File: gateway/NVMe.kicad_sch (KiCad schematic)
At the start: 0 parts

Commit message: Working on PCB
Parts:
- added C1401, C1402, C1411: 10u, Capacitor_SMD:C_0805_2012Metric, symbol Device:C
- added C1403, C1405, C1408, C1409: 100n, Capacitor_SMD:C_0402_1005Metric, symbol Device:C
- added C1404: 68n, Capacitor_SMD:C_0402_1005Metric, symbol Device:C
- added C1406: 150p, Capacitor_SMD:C_0402_1005Metric, symbol Device:C
- added C1407: 470u, Capacitor_SMD:CP_Elec_6.3x7.7, symbol Device:C_Polarized
- added C1410: 33p, Capacitor_SMD:C_0402_1005Metric, symbol Device:C
- added D1403: STPS3L60U, Diode_SMD:D_SMB, symbol ST:STPS3L60U
- added H1401: MountingHole, Wuerth:9774025151R, symbol Mechanical_Kampi:MountingHole
- added IC1402: ST1S14PHR, Package_SO:HSOP-8-1EP_3.9x4.9mm_P1.27mm_EP2.41x3.1mm, symbol ST:ST1S14PHR
- added L1401: 10u, Inductor_SMD:L_Wuerth_HCI-7050, symbol Device:L
- added LED1401: Power Good, LED_SMD:LED_0805_2012Metric, symbol Device:LED
- added MP1401: (no value), Bivar:SLP3-300-100-F, symbol Mechanical_Kampi:Light_Pipe
- added R1401, R1402: 100k, Resistor_SMD:R_0402_1005Metric, symbol Device:R
- added R1403: 150R, Resistor_SMD:R_0402_1005Metric, symbol Device:R
- added R1404: 82k5, Resistor_SMD:R_0402_1005Metric, symbol Device:R
- added R1405: 48k7, Resistor_SMD:R_0402_1005Metric, symbol Device:R
- added R1406: 4k7, Resistor_SMD:R_0805_2012Metric, symbol Device:R
- added TP1401, TP1402, TP1403: (no value), Testpoints_Kampi:TestPoint_Pad_1.0x1.0mm, symbol Connector:TestPoint
- added X1401: SSD, Amphenol:MDT420M03001, symbol Connector:Bus_M.2_Socket_M
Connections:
- new net: C1406.2, IC1402.4 (FB), R1404.2, R1405.1, TP1402.1
- new net: IC1402.3 (~{EN1}), R1402.1
- new net: LED1401.2 (A), R1403.2
- new net: C1405.1, D1403.1 (K), IC1402.8 (SW), L1401.1
- new net: C1405.2, IC1402.1 (BOOT)
- new net: IC1402.2 (PG), LED1401.1 (K)
- new net +1V8: R1406.1
- new net GND: C1401.2, C1402.2, C1403.2, C1404.2, C1407.2, C1408.2, C1409.2, C1410.2, C1411.2, D1403.2 (A), IC1402.6 (GND), IC1402.9 (EP), R1401.2, R1402.2, R1405.2, X1401.1 (GND), X1401.15 (GND), X1401.21 (GND), X1401.27 (GND), X1401.3 (GND), X1401.33 (GND), X1401.39 (GND), X1401.45 (GND), X1401.51 (GND), X1401.57 (GND), X1401.71 (GND), X1401.73 (GND), X1401.75 (GND), X1401.9 (GND)
- new net PCIe.CLK_N: X1401.53 (REFCLKn)
- new net PCIe.CLK_P: X1401.55 (REFCLKp)
- new net PCIe.RX_N: X1401.41 (PERn0/SATA-B+)
- new net PCIe.RX_P: X1401.43 (PERp0/SATA-B-)
- new net PCIe.TX_N: X1401.47 (PETn0/SATA-A-)
- new net PCIe.TX_P: X1401.49 (PETp0/SATA-A+)
- new net PCIe.~{CLK-REQ}: X1401.50 (~{PERST})
- new net PCIe.~{RST}: X1401.52 (~{CLKREQ})
- new net SSD-Power: IC1402.5 (EN2), R1401.1
- new net V_{In}: C1401.1, C1402.1, C1403.1, C1404.1, IC1402.7 (VIN), TP1401.1
- new net V_{SSD}: C1406.1, C1407.1, C1408.1, C1409.1, C1410.1, C1411.1, L1401.2, R1403.1, R1404.1, TP1403.1, X1401.12 (3.3V), X1401.14 (3.3V), X1401.16 (3.3V), X1401.18 (3.3V), X1401.2 (3.3V), X1401.4 (3.3V), X1401.70 (3.3V), X1401.72 (3.3V), X1401.74 (3.3V)
- new net ~{CTRL_WAKE1_MICO}: R1406.2, X1401.54 (~{PEWAKE})
- no-connect marks 0 -> 16

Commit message: Working on version 1.0.0
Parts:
- H1401: footprint Wuerth:9774025151R -> Wuerth:9774015151R; manf# 9774025151R -> 9774015151R; mouser# 710-9774025151R -> 710-9774015151R
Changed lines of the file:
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@@
 			)
 		)
-		(property "Datasheet" "https://cdn.amphenol-cs.com/media/wysiwyg/files/drawing/mdtxxxxxx001.pdf"
+		(property "Datasheet" "https://web.archive.org/web/20200613074028/http://read.pudn.com/downloads794/doc/project/3133918/PCIe_M.2_Electromechanical_Spec_Rev1.0_Final_11012013_RS_Clean.pdf#page=155"
 			(at 215.9 144.78 0)
 			(hide yes)
@@
 			)
 		)
-		(property "Footprint" "Wuerth:9774025151R"
+		(property "Footprint" "Wuerth:9774015151R"
 			(at 201.93 278.13 0)
 			(hide yes)
@@
 			)
 		)
-		(property "Datasheet" "https://www.we-online.com/components/products/datasheet/9774025151R.pdf"
+		(property "Datasheet" "https://www.we-online.com/components/products/datasheet/9774015151R.pdf"
 			(at 201.93 278.13 0)
 			(hide yes)
@@
 			)
 		)
-		(property "manf#" "9774025151R"
+		(property "manf#" "9774015151R"
 			(at 201.93 278.13 0)
 			(hide yes)
@@
 			)
 		)
-		(property "mouser#" "710-9774025151R"
+		(property "mouser#" "710-9774015151R"
 			(at 201.93 278.13 0)
 			(hide yes)

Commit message: Working on version 1.0.0
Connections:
- net SSD-Power renamed SSD-Power-Enable
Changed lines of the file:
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@@
 		)
 	)
-	(hierarchical_label "SSD-Power"
+	(hierarchical_label "SSD-Power-Enable"
 		(shape input)
 		(at 64.77 124.46 180)

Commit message: Adding level shifter, update documentation
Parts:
- TP1401, TP1402, TP1403: value (none) -> ~
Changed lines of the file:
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@@
 			)
 		)
-		(property "Value" ""
+		(property "Value" "~"
 			(at 161.29 94.615 0)
 			(show_name no)
@@
 			)
 		)
-		(property "Value" ""
+		(property "Value" "~"
 			(at 62.23 66.675 0)
 			(show_name no)
@@
 			)
 		)
-		(property "Value" ""
+		(property "Value" "~"
 			(at 181.61 66.675 0)
 			(show_name no)

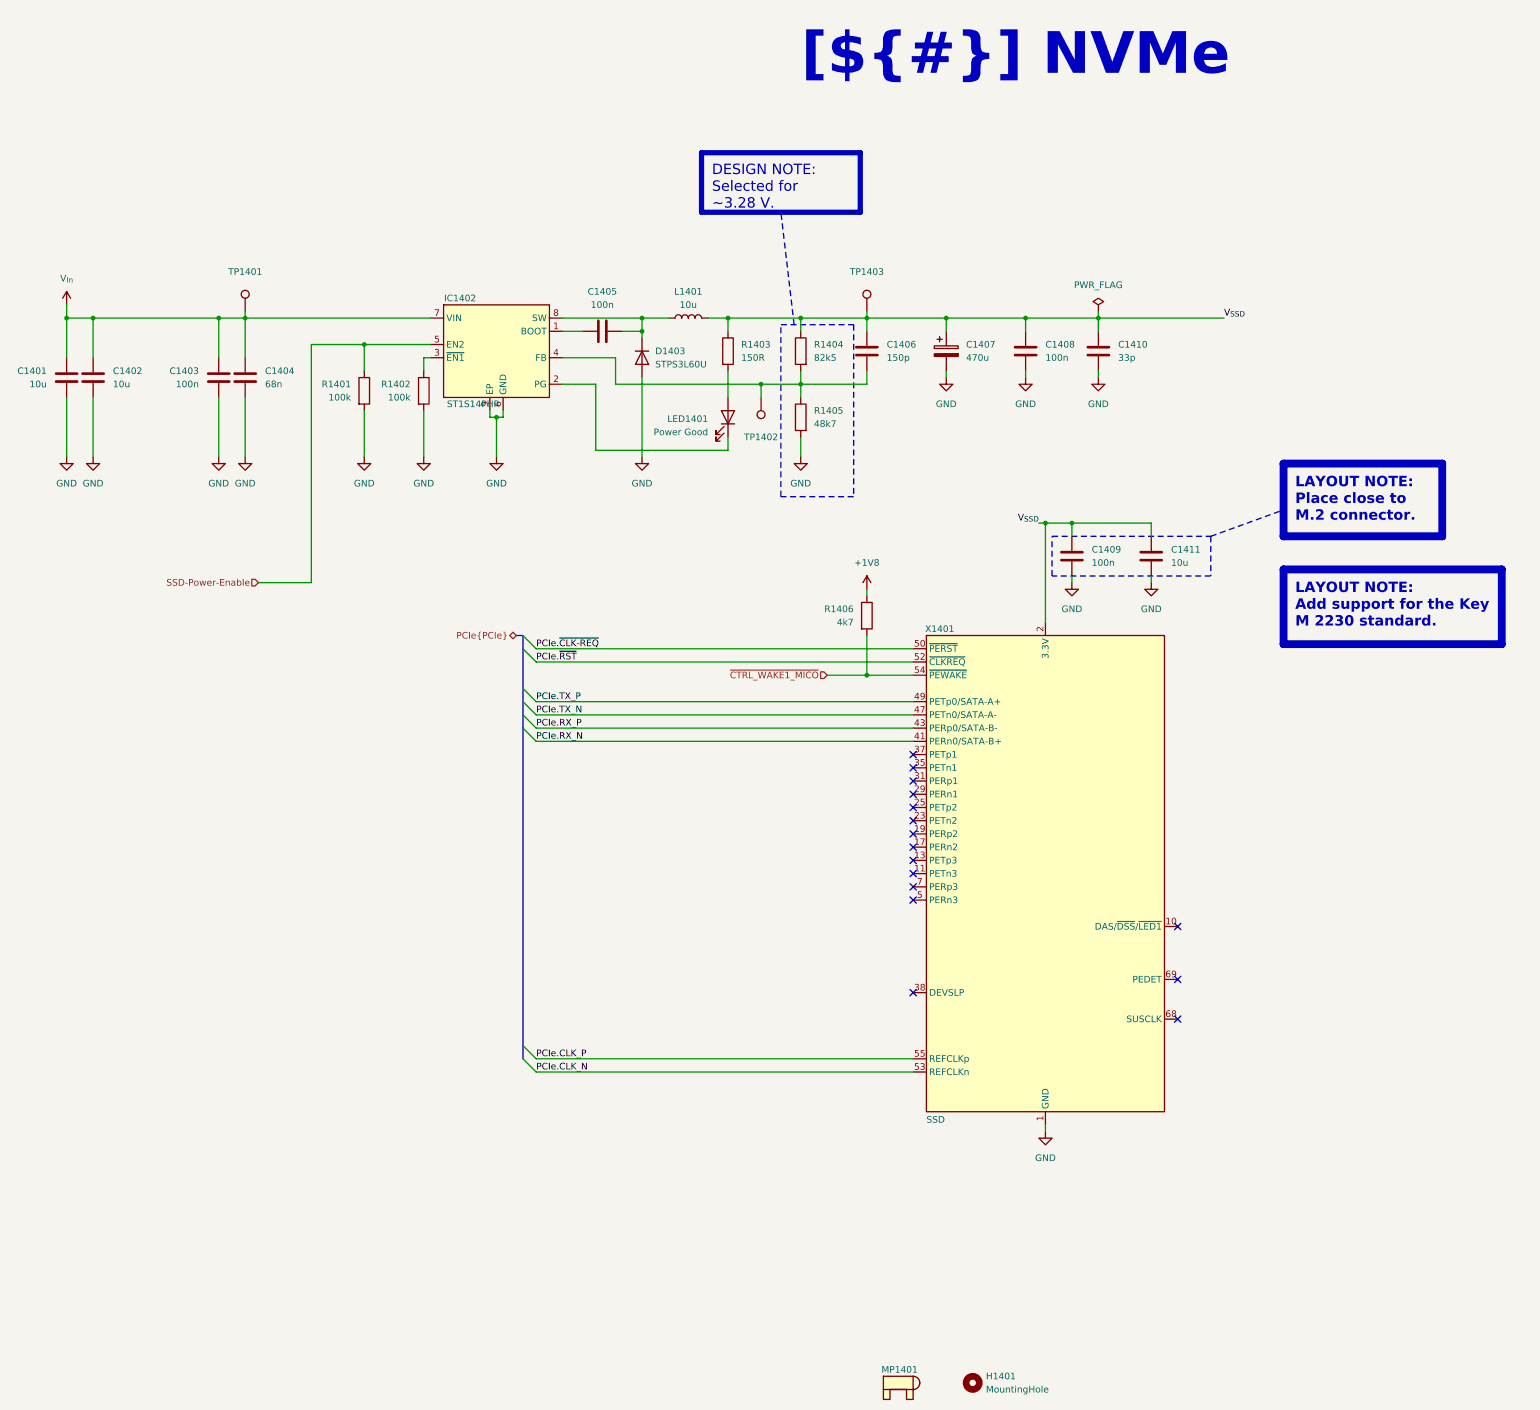
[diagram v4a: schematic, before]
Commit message: Replace level shifter, replace CC2530 with CC2652, fix wrong part numbers
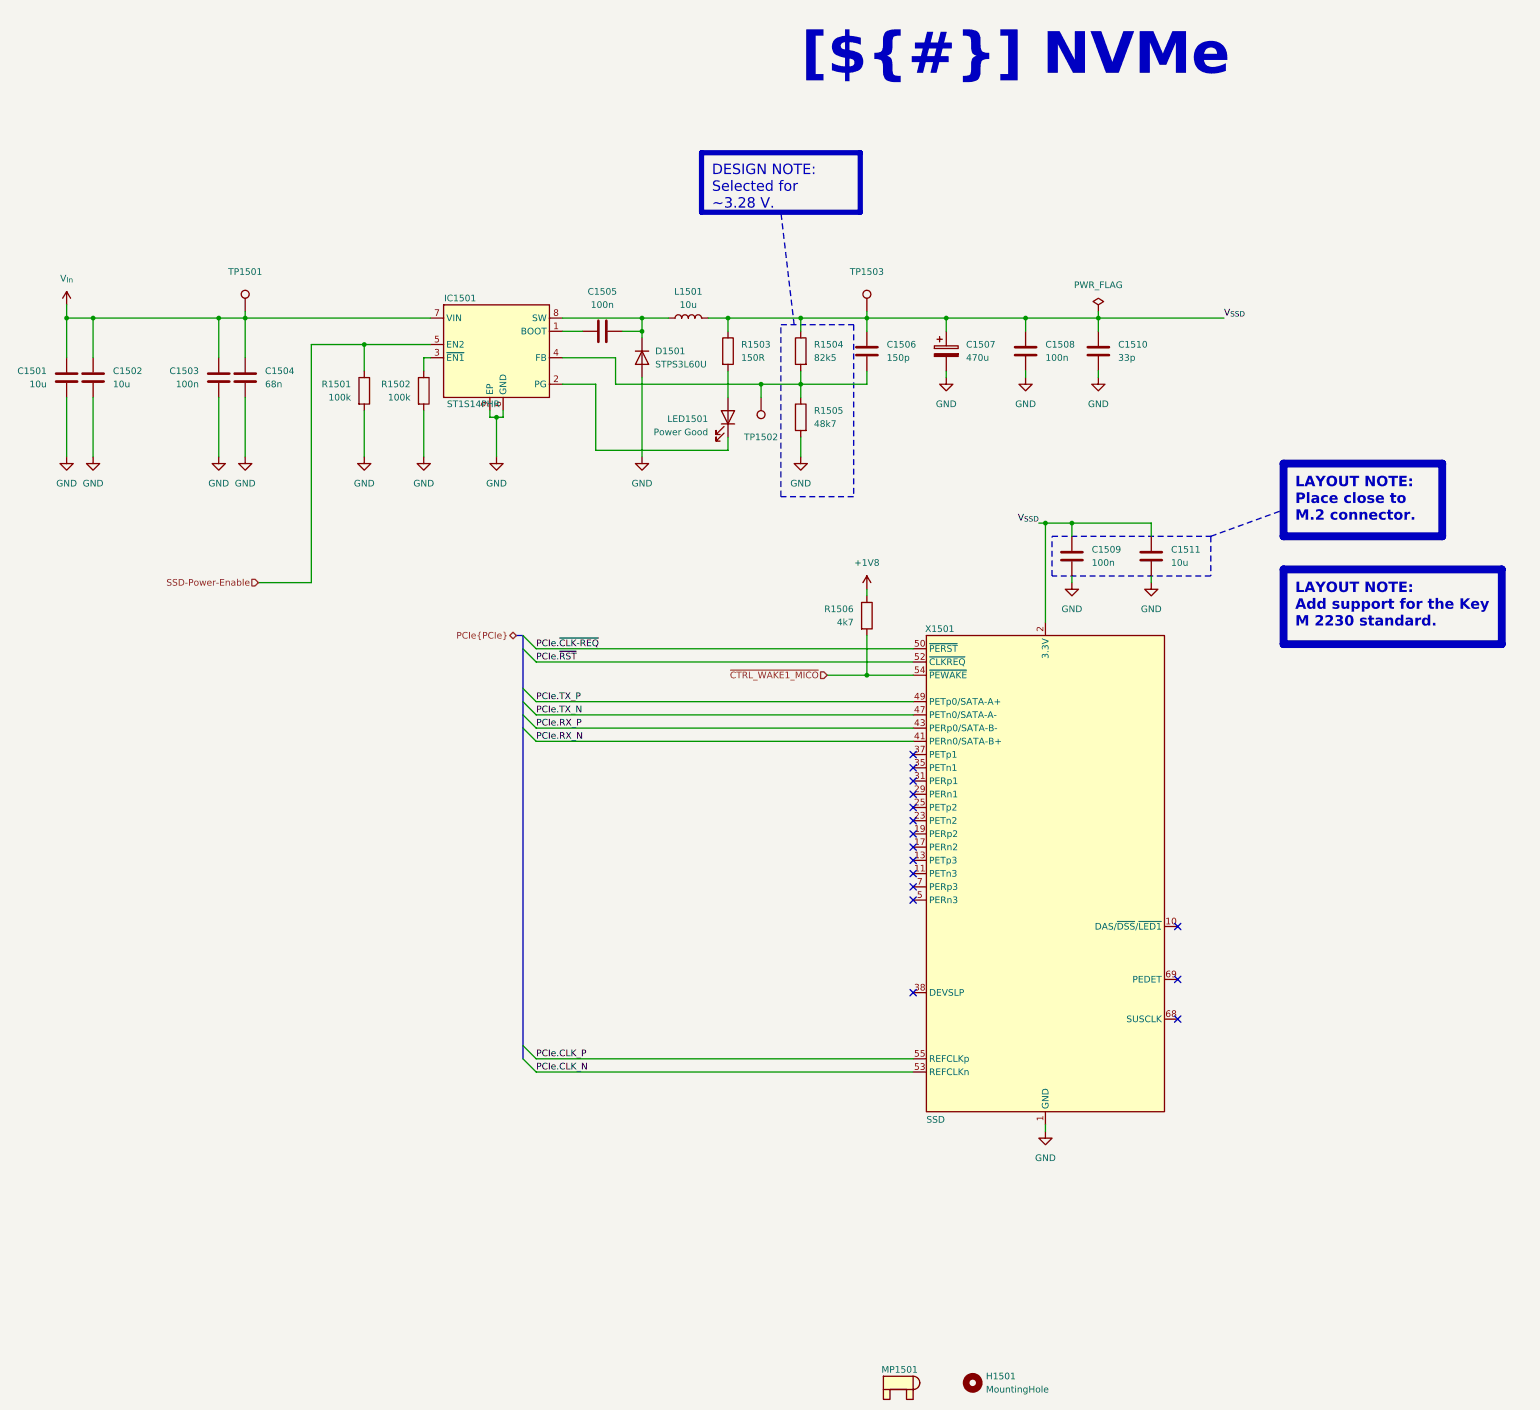
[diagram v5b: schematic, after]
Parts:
- C1503: renamed from C1403; footprint Capacitor_SMD:C_0402_1005Metric -> Capacitor_SMD:C_0805_2012Metric; manf# 04025C104JAT2A -> 08053C104M4T4A
- C1504: renamed from C1404; footprint Capacitor_SMD:C_0402_1005Metric -> Capacitor_SMD:C_0805_2012Metric; manf# 04025C683KAT2A -> 0805YC683KAT2A
- C1505: renamed from C1405; footprint Capacitor_SMD:C_0402_1005Metric -> Capacitor_SMD:C_0805_2012Metric; manf# 04025C104JAT2A -> 08053C104M4T4A
- C1506: renamed from C1406; footprint Capacitor_SMD:C_0402_1005Metric -> Capacitor_SMD:C_0805_2012Metric; manf# 04025C151MAT2A -> 08051U151JAT2A
- C1508: renamed from C1408; footprint Capacitor_SMD:C_0402_1005Metric -> Capacitor_SMD:C_0805_2012Metric; manf# 04025C104JAT2A -> 08053C104M4T4A
- C1509: renamed from C1409; footprint Capacitor_SMD:C_0402_1005Metric -> Capacitor_SMD:C_0805_2012Metric; manf# 04025C104JAT2A -> 08053C104M4T4A
- C1510: renamed from C1410; footprint Capacitor_SMD:C_0402_1005Metric -> Capacitor_SMD:C_0805_2012Metric; manf# 04021A330JAT2A -> 0805YA330JAT2A
- R1501: renamed from R1401; footprint Resistor_SMD:R_0402_1005Metric -> Resistor_SMD:R_0805_2012Metric; manf# CR0402-JW-104GLF -> CR0805-JW-104GLF
- R1502: renamed from R1402; footprint Resistor_SMD:R_0402_1005Metric -> Resistor_SMD:R_0805_2012Metric; manf# CR0402-JW-104GLF -> CR0805-JW-104GLF
- R1503: renamed from R1403; footprint Resistor_SMD:R_0402_1005Metric -> Resistor_SMD:R_0805_2012Metric; manf# CR0402-JW-151GLF -> CR0805-JW-151GLF
- R1504: renamed from R1404; footprint Resistor_SMD:R_0402_1005Metric -> Resistor_SMD:R_0805_2012Metric; manf# CR0402-FX-8252GLF -> CR0805-JW-8252GLF
- R1505: renamed from R1405; footprint Resistor_SMD:R_0402_1005Metric -> Resistor_SMD:R_0805_2012Metric; manf# CR0402-FX-4872GLF -> CR0805-JW-4872GLF
- renumbered C1401 to C1501, C1402 to C1502, C1407 to C1507, C1411 to C1511, D1403 to D1501, H1401 to H1501, IC1402 to IC1501, L1401 to L1501, LED1401 to LED1501, MP1401 to MP1501, R1406 to R1506, TP1401 to TP1501, TP1402 to TP1502, TP1403 to TP1503, X1401 to X1501
